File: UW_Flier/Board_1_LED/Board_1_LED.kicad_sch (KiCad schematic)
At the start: 11 parts, among them J1 RESET, J2 SWDIO, J3 SWDCLK, J4 GND, J5 VDD, J6 LED_DRAIN, Q1 CSD13385F5, U1 EYSHSNZWZ_module_stub

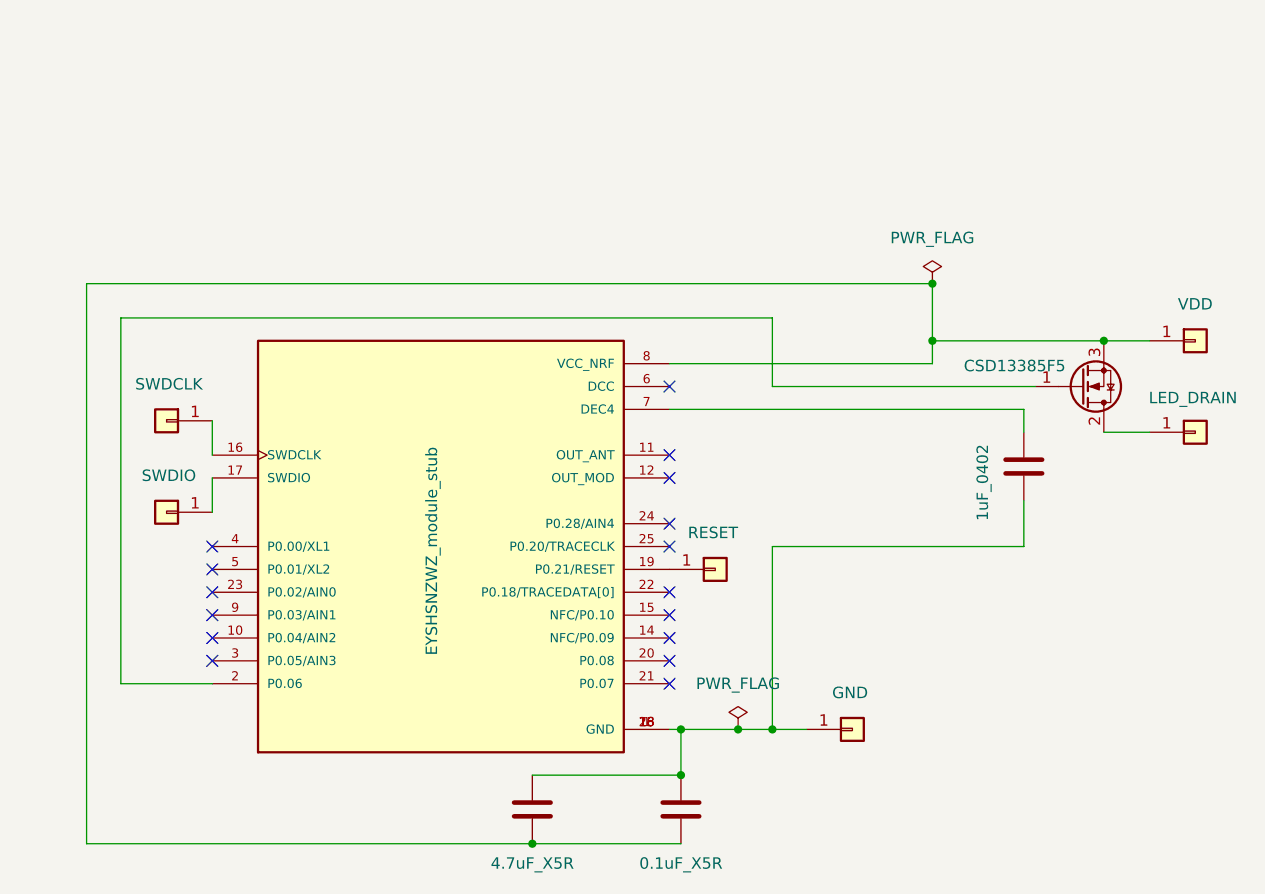
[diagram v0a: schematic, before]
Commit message: first iteration of PCB 1 (testing with mosfet / LED)
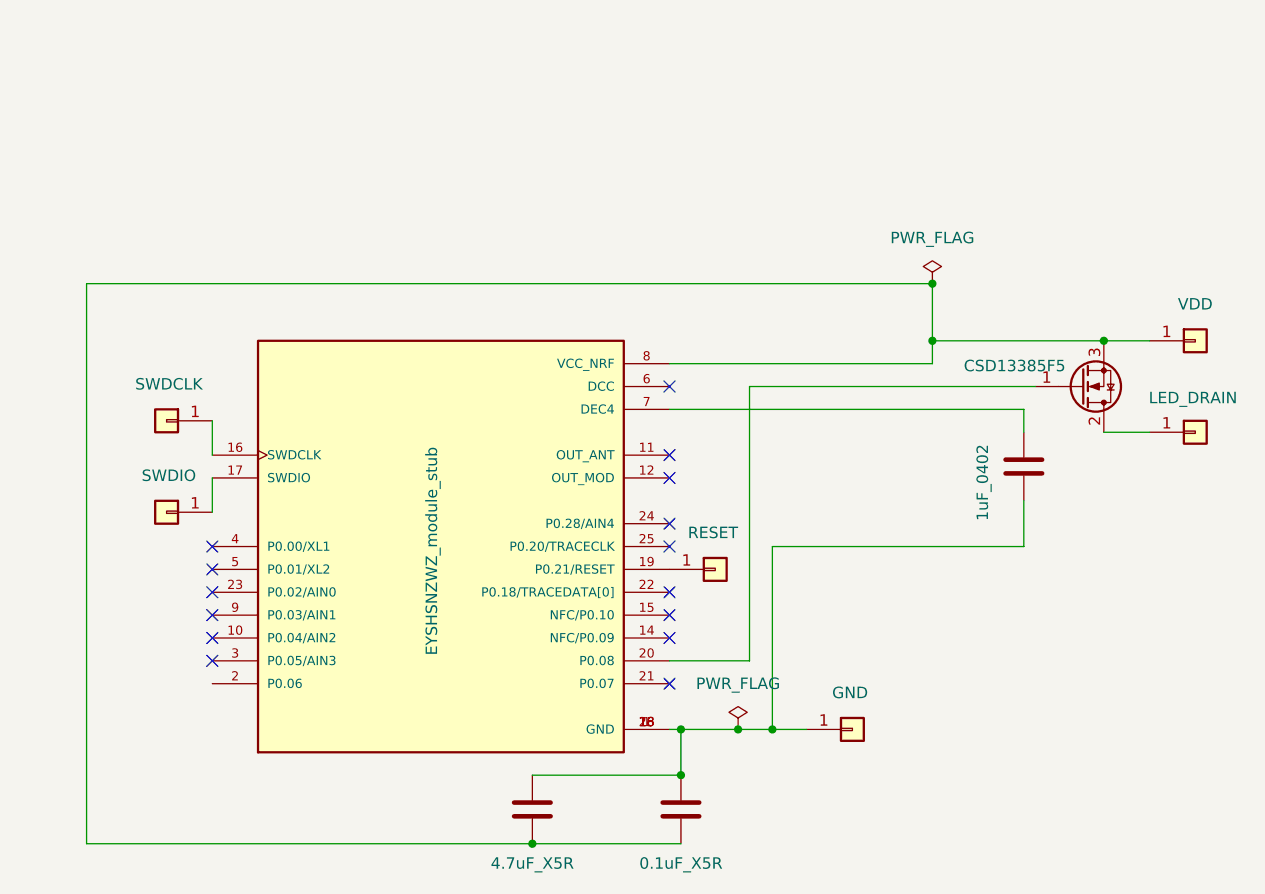
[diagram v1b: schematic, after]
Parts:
- Q1: footprint Package_DFN_QFN:Texas_PicoStar_DFN-3_0.69x0.60mm -> CSD13385F5:TRANS_CSD13385F5
- U1: footprint RF_Module:Taiyo-Yuden_EYSGJNZWY -> EYSHSNZWZ:XCVR_EYSHSNZWZ
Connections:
- net at U1.2 (P0.06): no longer Q1.1 (G)
- net at U1.20 (P0.08): now also Q1.1 (G)
- no-connect marks 16 -> 15
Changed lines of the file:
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@@
-	)
-	(no_connect
-		(at 96.52 85.09)
 	)
 	(no_connect
@@
 	(wire
 		(pts
-			(xy 107.95 54.61) (xy 137.16 54.61)
-		)
-		(stroke
-			(width 0)
-			(type default)
-		)
-	)
-	(wire
-		(pts
 			(xy 125.73 43.18) (xy 125.73 49.53)
 		)
@@
 	(wire
 		(pts
-			(xy 35.56 87.63) (xy 35.56 46.99)
-		)
-		(stroke
-			(width 0)
-			(type default)
-		)
-	)
-	(wire
-		(pts
 			(xy 81.28 105.41) (xy 31.75 105.41)
 		)
@@
 	(wire
 		(pts
-			(xy 107.95 46.99) (xy 107.95 54.61)
-		)
-		(stroke
-			(width 0)
-			(type default)
-		)
-	)
-	(wire
-		(pts
 			(xy 96.52 52.07) (xy 125.73 52.07)
 		)
@@
 	(wire
 		(pts
-			(xy 45.72 87.63) (xy 35.56 87.63)
-		)
-		(stroke
-			(width 0)
-			(type default)
-		)
-	)
-	(wire
-		(pts
 			(xy 97.79 92.71) (xy 97.79 97.79)
 		)
@@
 	(wire
 		(pts
+			(xy 96.52 85.09) (xy 105.41 85.09)
+		)
+		(stroke
+			(width 0)
+			(type default)
+		)
+	)
+	(wire
+		(pts
 			(xy 96.52 92.71) (xy 97.79 92.71)
 		)
@@
 	(wire
 		(pts
-			(xy 35.56 46.99) (xy 107.95 46.99)
-		)
-		(stroke
-			(width 0)
-			(type default)
-		)
-	)
-	(wire
-		(pts
 			(xy 104.14 92.71) (xy 107.95 92.71)
 		)
@@
 	(wire
 		(pts
+			(xy 105.41 54.61) (xy 137.16 54.61)
+		)
+		(stroke
+			(width 0)
+			(type default)
+		)
+	)
+	(wire
+		(pts
 			(xy 135.89 57.15) (xy 135.89 59.69)
 		)
@@
 		(pts
 			(xy 125.73 52.07) (xy 125.73 49.53)
+		)
+		(stroke
+			(width 0)
+			(type default)
+		)
+	)
+	(wire
+		(pts
+			(xy 105.41 54.61) (xy 105.41 85.09)
 		)
 		(stroke
@@
 			)
 		)
-		(property "Footprint" "RF_Module:Taiyo-Yuden_EYSGJNZWY"
+		(property "Footprint" "EYSHSNZWZ:XCVR_EYSHSNZWZ"
 			(at 71.12 72.39 0)
 			(effects
@@
 			)
 		)
-		(property "Footprint" "Package_DFN_QFN:Texas_PicoStar_DFN-3_0.69x0.60mm"
+		(property "Footprint" "CSD13385F5:TRANS_CSD13385F5"
 			(at 147.32 57.15 0)
 			(effects

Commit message: stuff
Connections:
- net at C1.2, C2.2, C3.2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: now also Q1.3 (S)
- net at C1.1, C2.1, J5.1 (Pin_1)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: no longer Q1.3 (S)
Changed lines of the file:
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@@
+	)
+	(junction
+		(at 119.38 43.18)
+		(diameter 0)
+		(color 0 0 0 0)
 	)
 	(junction
@@
 	)
 	(junction
-		(at 144.78 49.53)
-		(diameter 0)
-		(color 0 0 0 0)
-	)
-	(junction
 		(at 107.95 92.71)
-		(diameter 0)
-		(color 0 0 0 0)
-	)
-	(junction
-		(at 125.73 49.53)
 		(diameter 0)
 		(color 0 0 0 0)
@@
 	)
 	(junction
+		(at 107.95 80.01)
+		(diameter 0)
+		(color 0 0 0 0)
+	)
+	(junction
 		(at 97.79 97.79)
 		(diameter 0)
@@
 	(wire
 		(pts
-			(xy 125.73 43.18) (xy 125.73 49.53)
+			(xy 125.73 43.18) (xy 125.73 52.07)
 		)
 		(stroke
@@
 	(wire
 		(pts
+			(xy 140.97 41.91) (xy 125.73 41.91)
+		)
+		(stroke
+			(width 0)
+			(type default)
+		)
+	)
+	(wire
+		(pts
 			(xy 31.75 105.41) (xy 31.75 43.18)
 		)
@@
 	(wire
 		(pts
-			(xy 144.78 59.69) (xy 149.86 59.69)
-		)
-		(stroke
-			(width 0)
-			(type default)
-		)
-	)
-	(wire
-		(pts
 			(xy 135.89 67.31) (xy 135.89 72.39)
 		)
@@
 	(wire
 		(pts
+			(xy 125.73 41.91) (xy 125.73 43.18)
+		)
+		(stroke
+			(width 0)
+			(type default)
+		)
+	)
+	(wire
+		(pts
 			(xy 97.79 92.71) (xy 104.14 92.71)
 		)
@@
 	(wire
 		(pts
-			(xy 125.73 49.53) (xy 144.78 49.53)
+			(xy 138.43 93.98) (xy 138.43 90.17)
+		)
+		(stroke
+			(width 0)
+			(type default)
+		)
+	)
+	(wire
+		(pts
+			(xy 107.95 80.01) (xy 138.43 80.01)
+		)
+		(stroke
+			(width 0)
+			(type default)
+		)
+	)
+	(wire
+		(pts
+			(xy 107.95 80.01) (xy 107.95 92.71)
 		)
 		(stroke
@@
 	(wire
 		(pts
-			(xy 144.78 49.53) (xy 149.86 49.53)
-		)
-		(stroke
-			(width 0)
-			(type default)
-		)
-	)
-	(wire
-		(pts
 			(xy 96.52 52.07) (xy 125.73 52.07)
 		)
@@
 	(wire
 		(pts
+			(xy 146.05 93.98) (xy 138.43 93.98)
+		)
+		(stroke
+			(width 0)
+			(type default)
+		)
+	)
+	(wire
+		(pts
+			(xy 119.38 43.18) (xy 125.73 43.18)
+		)
+		(stroke
+			(width 0)
+			(type default)
+		)
+	)
+	(wire
+		(pts
 			(xy 97.79 92.71) (xy 97.79 97.79)
 		)
@@
 	(wire
 		(pts
-			(xy 107.95 72.39) (xy 107.95 92.71)
+			(xy 107.95 72.39) (xy 107.95 80.01)
 		)
 		(stroke
@@
 	(wire
 		(pts
-			(xy 96.52 85.09) (xy 105.41 85.09)
+			(xy 96.52 85.09) (xy 130.81 85.09)
 		)
 		(stroke
@@
 	(wire
 		(pts
-			(xy 31.75 43.18) (xy 125.73 43.18)
-		)
-		(stroke
-			(width 0)
-			(type default)
-		)
-	)
-	(wire
-		(pts
-			(xy 105.41 54.61) (xy 137.16 54.61)
+			(xy 31.75 43.18) (xy 119.38 43.18)
 		)
 		(stroke
@@
 		(pts
 			(xy 135.89 57.15) (xy 135.89 59.69)
-		)
-		(stroke
-			(width 0)
-			(type default)
-		)
-	)
-	(wire
-		(pts
-			(xy 125.73 52.07) (xy 125.73 49.53)
-		)
-		(stroke
-			(width 0)
-			(type default)
-		)
-	)
-	(wire
-		(pts
-			(xy 105.41 54.61) (xy 105.41 85.09)
 		)
 		(stroke
@@
 	(symbol
 		(lib_id "power:PWR_FLAG")
-		(at 125.73 43.18 0)
+		(at 119.38 43.18 0)
 		(unit 1)
 		(exclude_from_sim no)
@@
 		(fields_autoplaced yes)
 		(property "Reference" "#FLG01"
-			(at 125.73 41.275 0)
+			(at 119.38 41.275 0)
 			(effects
 				(font
@@
 		)
 		(property "Value" "PWR_FLAG"
-			(at 125.73 38.1 0)
+			(at 119.38 38.1 0)
 			(effects
 				(font
@@
 		)
 		(property "Footprint" ""
-			(at 125.73 43.18 0)
+			(at 119.38 43.18 0)
 			(effects
 				(font
@@
 		)
 		(property "Datasheet" "~"
-			(at 125.73 43.18 0)
+			(at 119.38 43.18 0)
 			(effects
 				(font
@@
 		)
 		(property "Description" "Special symbol for telling ERC where power comes from"
-			(at 125.73 43.18 0)
+			(at 119.38 43.18 0)
 			(effects
 				(font
@@
 	(symbol
 		(lib_id "Connector_Generic:Conn_01x01")
-		(at 154.94 49.53 0)
+		(at 146.05 41.91 0)
 		(unit 1)
 		(exclude_from_sim no)
@@
 		(dnp no)
 		(property "Reference" "J5"
-			(at 154.94 46.53 0)
+			(at 146.05 38.91 0)
 			(effects
 				(font
@@
 		)
 		(property "Value" "VDD"
-			(at 154.94 45.466 0)
+			(at 146.05 37.846 0)
 			(effects
 				(font
@@
 		)
 		(property "Footprint" "TestPoint:TestPoint_Pad_2.0x2.0mm"
-			(at 154.94 49.53 0)
+			(at 146.05 41.91 0)
 			(effects
 				(font
@@
 		)
 		(property "Datasheet" "~"
-			(at 154.94 49.53 0)
+			(at 146.05 41.91 0)
 			(effects
 				(font
@@
 		)
 		(property "Description" "Generic connector, single row, 01x01, script generated (kicad-library-utils/schlib/autogen/connector/)"
-			(at 154.94 49.53 0)
+			(at 146.05 41.91 0)
 			(effects
 				(font
@@
 	(symbol
 		(lib_id "Connector_Generic:Conn_01x01")
-		(at 154.94 59.69 0)
+		(at 151.13 93.98 0)
 		(unit 1)
 		(exclude_from_sim no)
@@
 		(dnp no)
 		(property "Reference" "J6"
-			(at 154.94 56.69 0)
+			(at 151.13 90.98 0)
 			(effects
 				(font
@@
 		)
 		(property "Value" "LED_DRAIN"
-			(at 154.686 55.88 0)
+			(at 150.876 90.17 0)
 			(effects
 				(font
@@
 		)
 		(property "Footprint" "TestPoint:TestPoint_Pad_2.0x2.0mm"
-			(at 154.94 59.69 0)
+			(at 151.13 93.98 0)
 			(effects
 				(font
@@
 		)
 		(property "Datasheet" "~"
-			(at 154.94 59.69 0)
+			(at 151.13 93.98 0)
 			(effects
 				(font
@@
 		)
 		(property "Description" "Generic connector, single row, 01x01, script generated (kicad-library-utils/schlib/autogen/connector/)"
-			(at 154.94 59.69 0)
+			(at 151.13 93.98 0)
 			(effects
 				(font
@@
 	(symbol
 		(lib_id "Transistor_FET:Q_NMOS_GDS")
-		(at 142.24 54.61 0)
+		(at 135.89 85.09 0)
 		(mirror x)
 		(unit 1)
@@
 		(dnp no)
 		(property "Reference" "Q1"
-			(at 142.24 58.61 0)
+			(at 135.89 89.09 0)
 			(effects
 				(font
@@
 		)
 		(property "Value" "CSD13385F5"
-			(at 134.874 52.324 0)
+			(at 128.524 82.804 0)
 			(effects
 				(font
@@
 		)
 		(property "Footprint" "CSD13385F5:TRANS_CSD13385F5"
-			(at 147.32 57.15 0)
+			(at 140.97 87.63 0)
 			(effects
 				(font
@@
 		)
 		(property "Datasheet" "~"
-			(at 142.24 54.61 0)
+			(at 135.89 85.09 0)
 			(effects
 				(font
@@
 		)
 		(property "Description" "N-MOSFET transistor, gate/drain/source"
-			(at 142.24 54.61 0)
-			(effects
-				(font
+			(at 135.89 85.09 0)
+			(effects
+				(font

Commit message: updated PCB
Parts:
- C1: footprint Capacitor_SMD:C_0603_1608Metric -> Capacitor_SMD:C_0402_1005Metric
- J1, J2, J3, J4, J5, J6: footprint TestPoint:TestPoint_Pad_2.0x2.0mm -> CSD13385F5:TestPoint_Pad_1.5x1.5mm_2
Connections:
- net at C1.2, C2.2, C3.2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: now also Q1.2 (D); no longer Q1.3 (S)
- net at J6.1 (Pin_1): now also Q1.3 (S); no longer Q1.2 (D)
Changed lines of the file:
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@@
+	)
+	(junction
+		(at 107.95 80.01)
+		(diameter 0)
+		(color 0 0 0 0)
 	)
 	(junction
@@
 	)
 	(junction
-		(at 107.95 80.01)
-		(diameter 0)
-		(color 0 0 0 0)
-	)
-	(junction
 		(at 97.79 97.79)
 		(diameter 0)
@@
 	(wire
 		(pts
+			(xy 138.43 90.17) (xy 138.43 93.98)
+		)
+		(stroke
+			(width 0)
+			(type default)
+		)
+	)
+	(wire
+		(pts
 			(xy 140.97 41.91) (xy 125.73 41.91)
 		)
@@
 	(wire
 		(pts
-			(xy 138.43 93.98) (xy 138.43 90.17)
+			(xy 107.95 72.39) (xy 107.95 80.01)
+		)
+		(stroke
+			(width 0)
+			(type default)
+		)
+	)
+	(wire
+		(pts
+			(xy 45.72 58.42) (xy 45.72 62.23)
+		)
+		(stroke
+			(width 0)
+			(type default)
+		)
+	)
+	(wire
+		(pts
+			(xy 135.89 72.39) (xy 107.95 72.39)
+		)
+		(stroke
+			(width 0)
+			(type default)
+		)
+	)
+	(wire
+		(pts
+			(xy 96.52 57.15) (xy 135.89 57.15)
 		)
 		(stroke
@@
 	(wire
 		(pts
-			(xy 45.72 58.42) (xy 45.72 62.23)
-		)
-		(stroke
-			(width 0)
-			(type default)
-		)
-	)
-	(wire
-		(pts
-			(xy 135.89 72.39) (xy 107.95 72.39)
-		)
-		(stroke
-			(width 0)
-			(type default)
-		)
-	)
-	(wire
-		(pts
-			(xy 96.52 57.15) (xy 135.89 57.15)
-		)
-		(stroke
-			(width 0)
-			(type default)
-		)
-	)
-	(wire
-		(pts
 			(xy 96.52 52.07) (xy 125.73 52.07)
 		)
@@
 		(pts
 			(xy 97.79 92.71) (xy 97.79 97.79)
-		)
-		(stroke
-			(width 0)
-			(type default)
-		)
-	)
-	(wire
-		(pts
-			(xy 107.95 72.39) (xy 107.95 80.01)
 		)
 		(stroke
@@
 			)
 		)
-		(property "Footprint" "TestPoint:TestPoint_Pad_2.0x2.0mm"
+		(property "Footprint" "CSD13385F5:TestPoint_Pad_1.5x1.5mm_2"
 			(at 40.64 58.42 0)
 			(effects
@@
 			)
 		)
-		(property "Footprint" "TestPoint:TestPoint_Pad_2.0x2.0mm"
+		(property "Footprint" "CSD13385F5:TestPoint_Pad_1.5x1.5mm_2"
 			(at 146.05 41.91 0)
 			(effects
@@
 			)
 		)
-		(property "Footprint" "TestPoint:TestPoint_Pad_2.0x2.0mm"
+		(property "Footprint" "CSD13385F5:TestPoint_Pad_1.5x1.5mm_2"
 			(at 116.84 92.71 0)
 			(effects
@@
 			)
 		)
-		(property "Footprint" "Capacitor_SMD:C_0603_1608Metric"
+		(property "Footprint" "Capacitor_SMD:C_0402_1005Metric"
 			(at 82.2452 97.79 0)
 			(effects
@@
 			)
 		)
-		(property "Footprint" "TestPoint:TestPoint_Pad_2.0x2.0mm"
+		(property "Footprint" "CSD13385F5:TestPoint_Pad_1.5x1.5mm_2"
 			(at 101.6 74.93 0)
 			(effects
@@
 			)
 		)
-		(property "Footprint" "TestPoint:TestPoint_Pad_2.0x2.0mm"
+		(property "Footprint" "CSD13385F5:TestPoint_Pad_1.5x1.5mm_2"
 			(at 40.64 68.58 0)
 			(effects
@@
 			)
 		)
-		(property "Footprint" "TestPoint:TestPoint_Pad_2.0x2.0mm"
+		(property "Footprint" "CSD13385F5:TestPoint_Pad_1.5x1.5mm_2"
 			(at 151.13 93.98 0)
 			(effects
@@
 		(lib_id "Transistor_FET:Q_NMOS_GDS")
 		(at 135.89 85.09 0)
-		(mirror x)
 		(unit 1)
 		(exclude_from_sim no)
@@
 		(dnp no)
 		(property "Reference" "Q1"
-			(at 135.89 89.09 0)
+			(at 135.89 81.09 0)
 			(effects
 				(font
@@
 		)
 		(property "Value" "CSD13385F5"
-			(at 128.524 82.804 0)
+			(at 128.524 87.376 0)
 			(effects
 				(font
@@
 		)
 		(property "Footprint" "CSD13385F5:TRANS_CSD13385F5"
-			(at 140.97 87.63 0)
-			(effects
-				(font
+			(at 140.97 82.55 0)
+			(effects
+				(font

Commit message: stuff (thursday before leaving)
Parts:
- added C4, C5: C, Capacitor_SMD:C_0201_0603Metric_Pad0.64x0.40mm_HandSolder, symbol Device:C
- added Y1: Crystal, Capacitor_SMD:C_0402_1005Metric, symbol Device:Crystal
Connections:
- net at C1.2, C2.2, C3.2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: now also C4.2, C5.2
- net at U1.4 (P0.00/XL1): now also C5.1, Y1.1
- net at U1.5 (P0.01/XL2): now also C4.1, Y1.2
- no-connect marks 15 -> 13

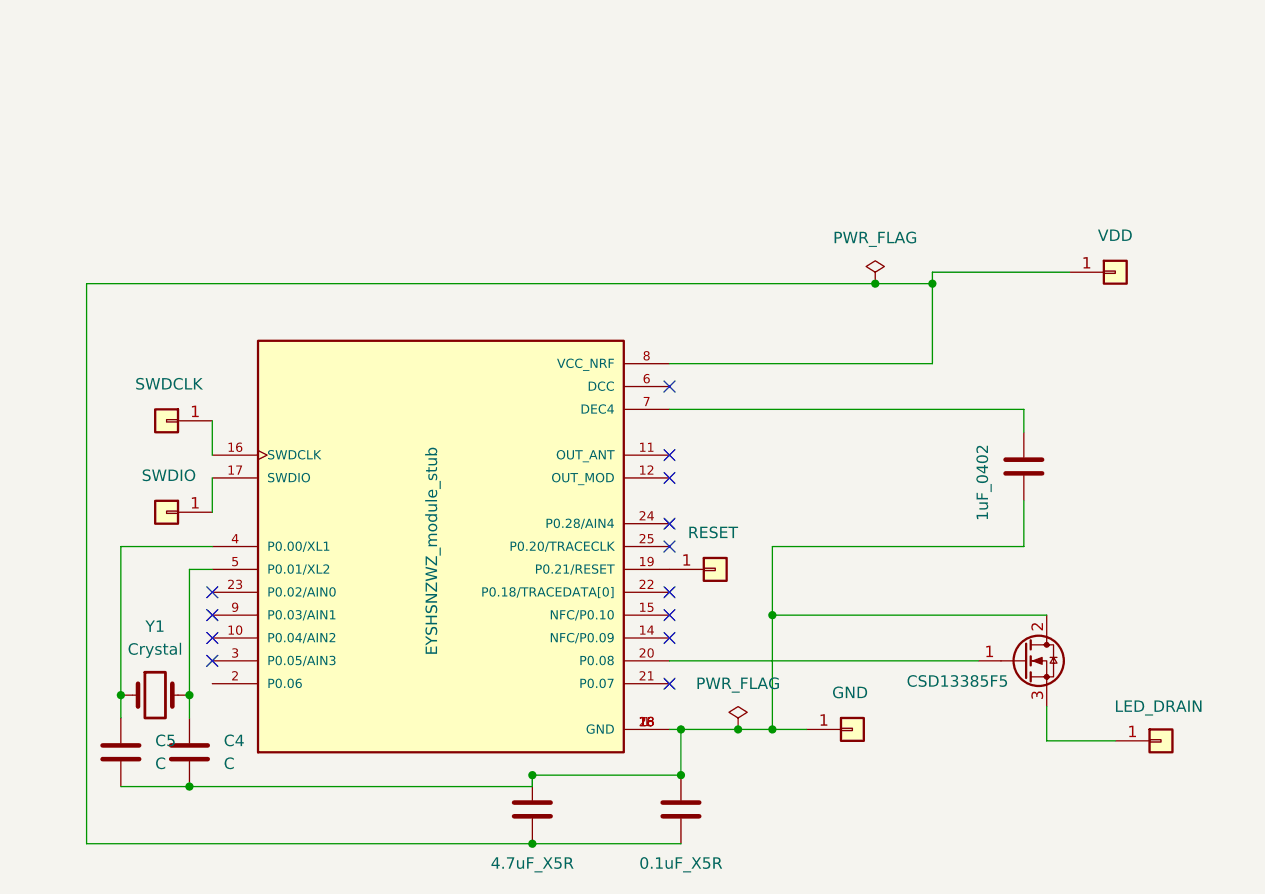
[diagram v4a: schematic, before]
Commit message: added bmp384
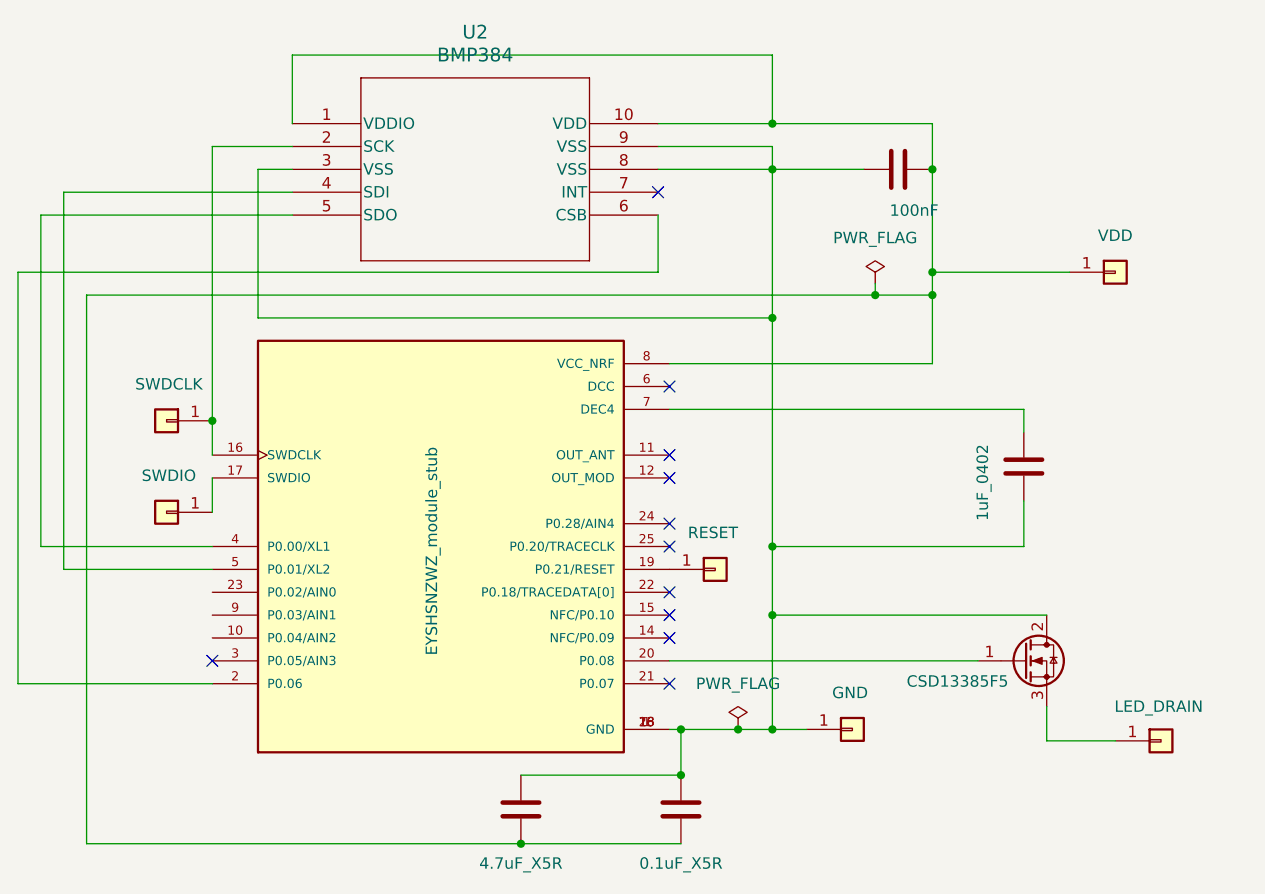
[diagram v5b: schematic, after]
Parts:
- removed C4, C5: C, Capacitor_SMD:C_0201_0603Metric_Pad0.64x0.40mm_HandSolder, symbol Device:C
- removed Y1: Crystal, Capacitor_SMD:C_0402_1005Metric, symbol Device:Crystal
- added C6: 100nF, Capacitor_SMD:C_0402_1005Metric, symbol Device:C
- added U2: BMP384, footprints:LGA10_2.0X2.0X0.95_BOS, symbol 2025-11-18_15-02-21:BMP384
- J1, J2, J3, J4, J5, J6: footprint CSD13385F5:TestPoint_Pad_1.5x1.5mm_2 -> TestPoint:TestPoint_Pad_1.0x1.0mm
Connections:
- net at C1.2, C2.2, C3.2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: now also C6.1, U2.3 (VSS), U2.8 (VSS), U2.9 (VSS)
- net at U1.4 (P0.00/XL1): now also U2.5 (SDO)
- net at U1.5 (P0.01/XL2): now also U2.4 (SDI)
- net at C1.1, C2.1, J5.1 (Pin_1)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: now also C6.2, U2.1 (VDDIO), U2.10 (VDD)
- net at J3.1 (Pin_1), U1.16 (SWDCLK): now also U2.2 (SCK)
- net at U1.2 (P0.06): now also U2.6 (CSB)
- no-connect marks 13 -> 11
